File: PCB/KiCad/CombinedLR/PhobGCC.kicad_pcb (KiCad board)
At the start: 2 copper layers, 147.6 x 91.4 mm, 82 parts, among them J1 Conn_01x06_Female, J2 Conn_01x04_Female, J3 Conn_01x01_Male, J4 Conn_01x04_Male, J5 Rumble, J6 L, J7 R, Q1 Q_NMOS_GSD, Q2 Q_PMOS_GDS, Q3 Q_NMOS_GSD, SW1 A, SW10 Dup, SW11 Dright, SW12 Ddown, SW13 L, SW14 R, SW2 B, SW3 X, SW4 Y, SW5 Start, SW6 L, SW7 R, SW8 Z, SW9 Dleft, U1 Teensy4.0, U2 2x DRV5053CAQLPGM Hall Effect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, U3 GP2S60-MFG, U4 GP2S60-MFG, U5 Stickbox_Assembly

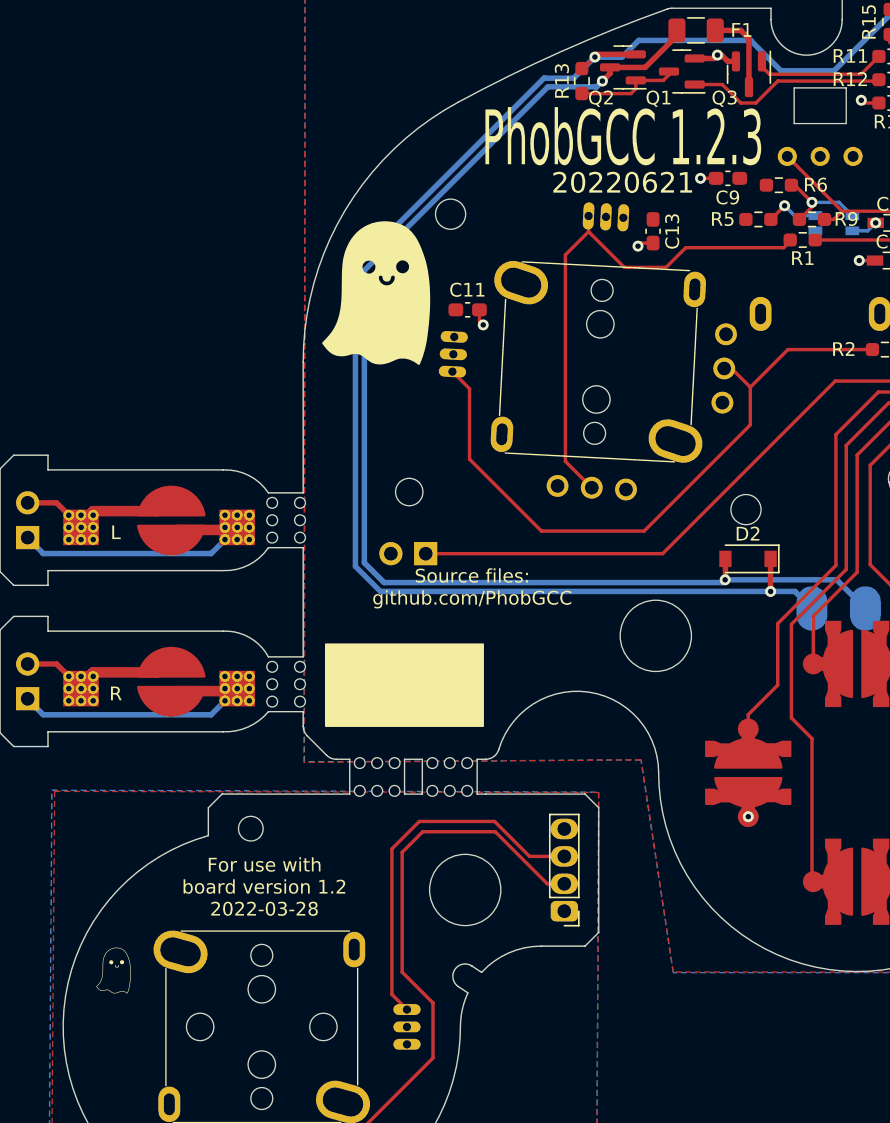
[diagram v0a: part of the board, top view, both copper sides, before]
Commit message: Replace PhobGCC text/logos with BealeGCC & BG logo
Add full Beale Gaming (BG) logo and small BG logo png files. Convert
these into two kicad_mod files: a 10mm footprint for the full logo and a
4mm footprint for the small logo. On the CombinedLR PCB, replace the
large ghost with the full logo, the small ghost with the small logo, and
the "PhobGCC" text with "BealeGCC". The Motherboard, CStick, and
Combined PCBs are unchanged. Update the README to say "BealeGCC".
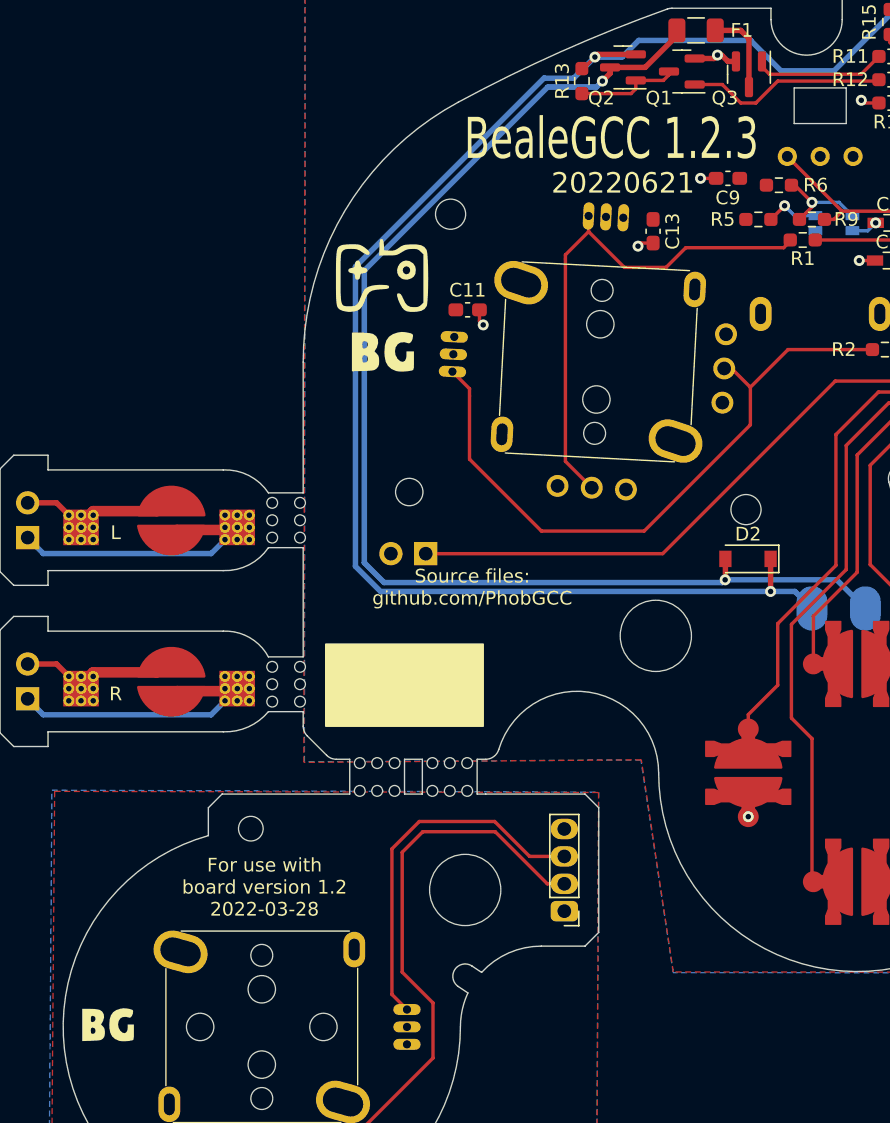
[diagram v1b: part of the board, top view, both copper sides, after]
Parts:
- removed the G*** at (53.8, 46.2)
- removed the G*** at (34.5, 95.6)
- added G***: LOGO, PhobGCC_Footprints:BealeGamingSmall4mm, F.Cu at (34.0, 99.5)
- added G***: LOGO, PhobGCC_Footprints:BealeGamingFull10mm, F.Cu at (54.0, 47.0)
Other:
- board text added: "BealeGCC 1.2.3"
- board text removed: "PhobGCC 1.2.3"
